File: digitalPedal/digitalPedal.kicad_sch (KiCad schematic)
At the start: 17 parts, among them J1 ACJS-MV-3, J2 ACJS-MV-3, J3 Barrel_Jack_Switch, SW1 3PDT, U1 Teensy4.1, U2 LM2596T-ADJ

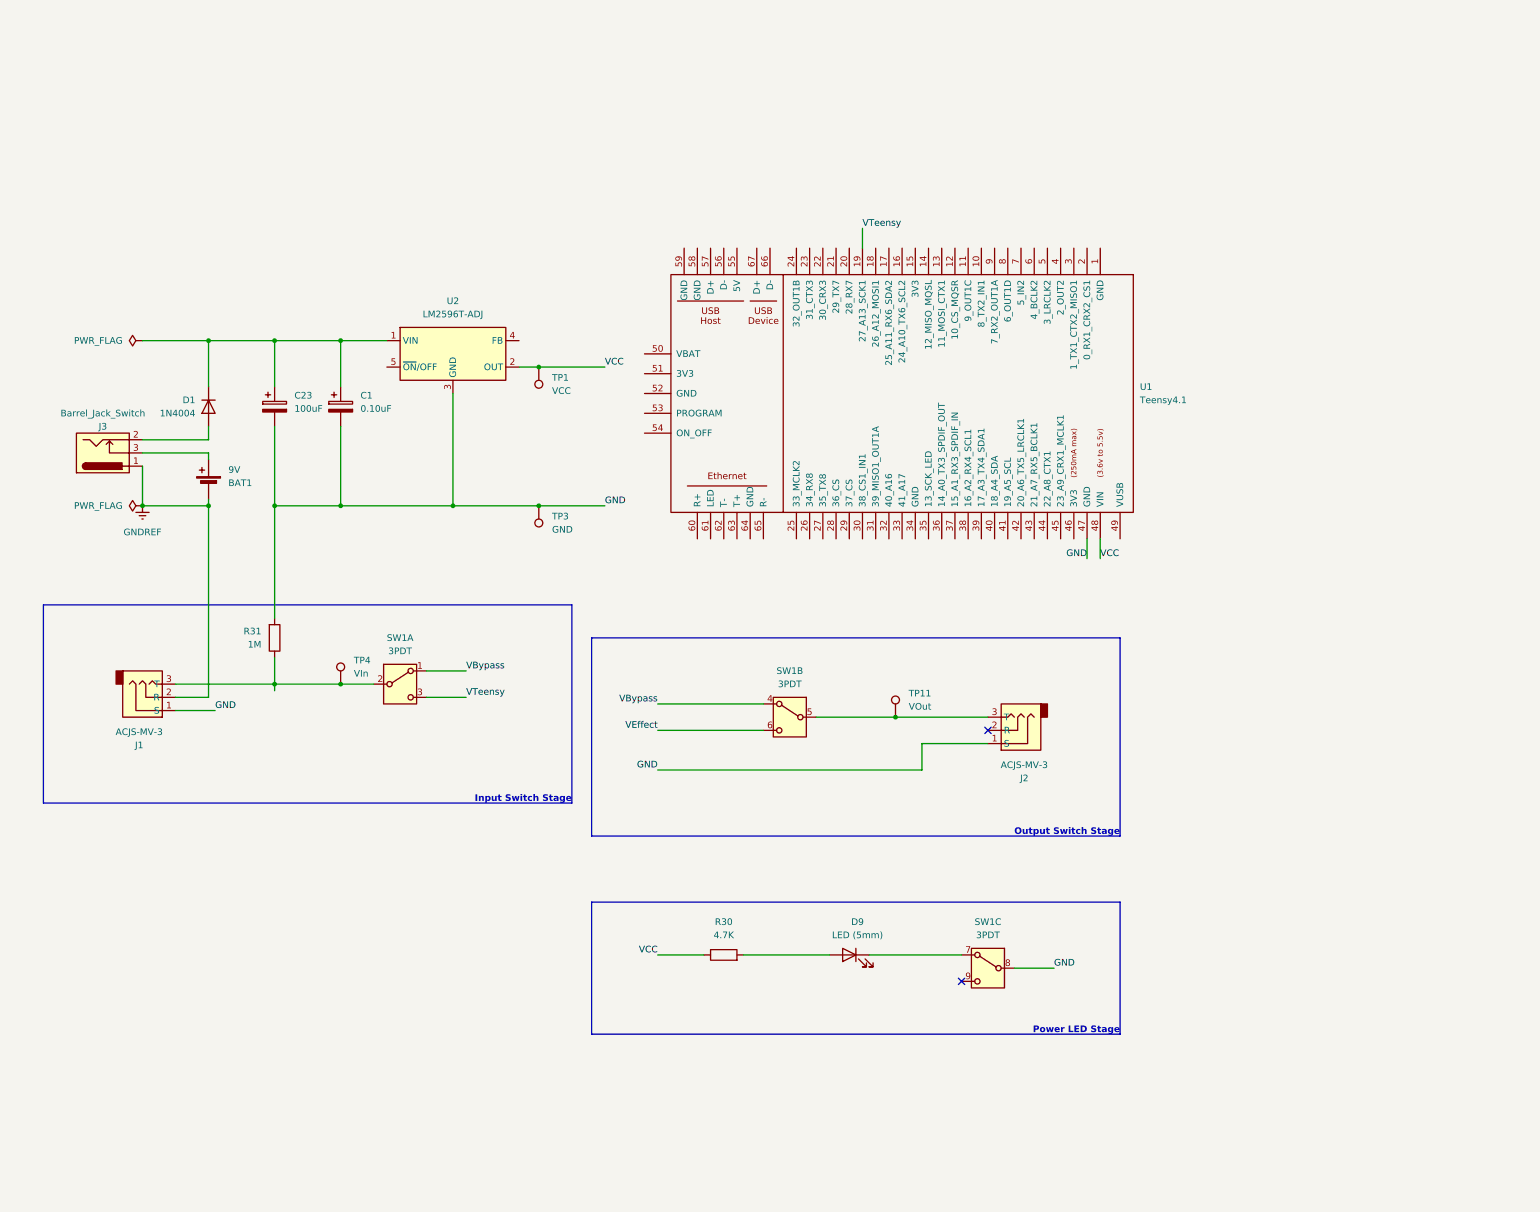
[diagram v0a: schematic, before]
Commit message: Updates to digital pedal circuti
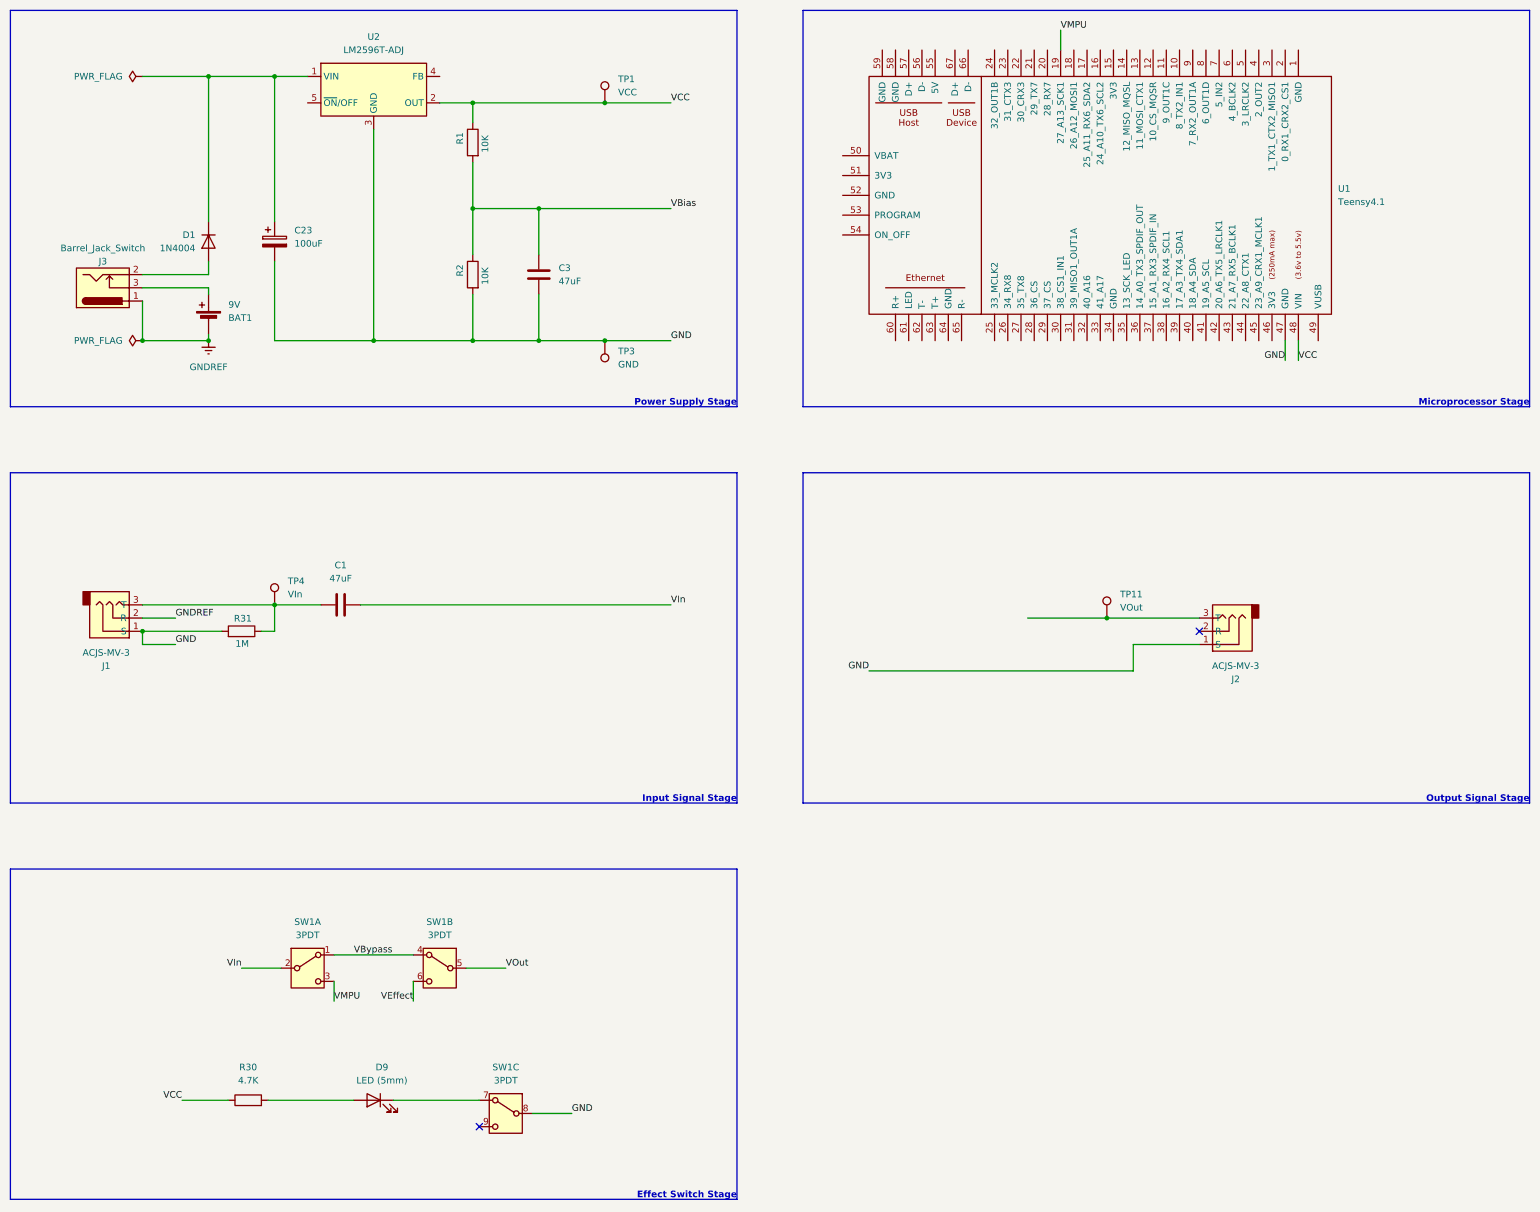
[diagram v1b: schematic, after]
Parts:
- removed C1: 0.10uF, Capacitor_THT:C_Radial_D5.0mm_H11.0mm_P2.00mm, symbol Device:C_Polarized
- added C1, C3: 47uF, symbol Device:C
- added R1, R2: 10K, Resistor_THT:R_Axial_DIN0207_L6.3mm_D2.5mm_P7.62mm_Horizontal, symbol Device:R
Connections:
- net GND: now also C3.2, R2.2
- net VCC: now also R1.1
- net at J2.3 (T), TP11.1: no longer SW1.5
- net at J1.3 (T), R31.1, TP4.1: now also C1.1; no longer SW1.2
- net VTeensy renamed VMPU
- new net VBias: C3.1, R1.2, R2.1
- new net VIn: C1.2, SW1.2
- new net VOut: SW1.5
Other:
- note added: "Effect Switch Stage"
- note added: "Input Signal Stage"
- note added: "Microprocessor Stage"
- note added: "Output Signal Stage"
- note added: "Power Supply Stage"
- note removed: "Input Switch Stage"
- note removed: "Output Switch Stage"
- note removed: "Power LED Stage"
- moved on the sheet: BAT1, C23, D1, D9, J1, J2, J3, R30, R31, SW1A, SW1B, SW1C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
